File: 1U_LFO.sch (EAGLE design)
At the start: 22 parts

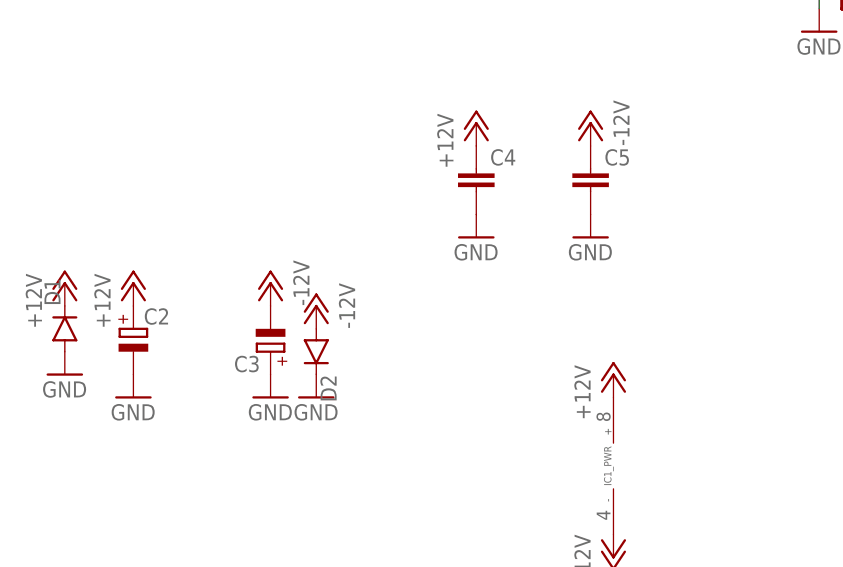
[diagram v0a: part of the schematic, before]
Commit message: 1U LFO
Basic Low Frequency Oscillator
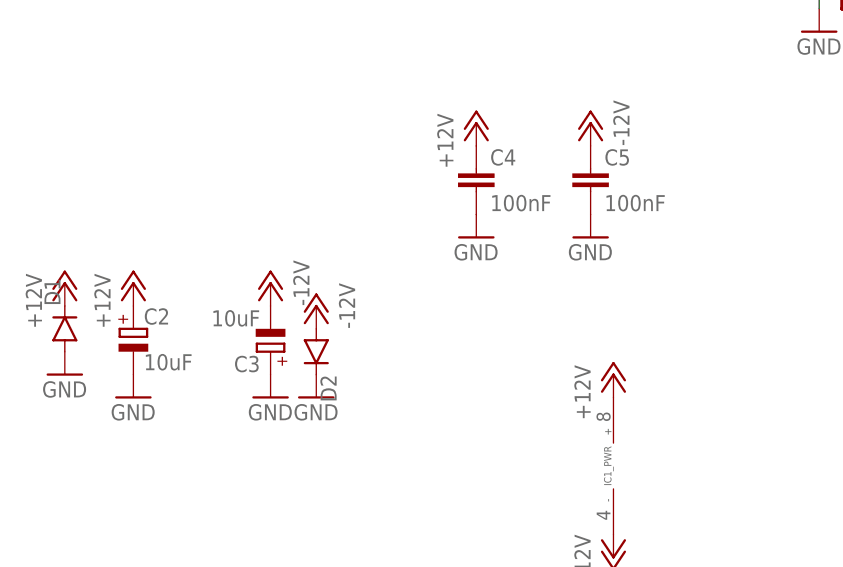
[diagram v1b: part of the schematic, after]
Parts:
- C2, C3: value (none) -> 10uF
- C4, C5: value (none) -> 100nF
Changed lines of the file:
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@@
 <?xml version="1.0" encoding="utf-8"?>
 <!DOCTYPE eagle SYSTEM "eagle.dtd">
-<eagle version="7.5.0">
+<eagle version="8.1.1">
 <drawing>
 <settings>
@@
 <part name="P-2" library="supply1" deviceset="-12V" device=""/>
 <part name="P-3" library="supply1" deviceset="-12V" device=""/>
-<part name="C2" library="dp_devices" deviceset="CAPACITOR_POL" device="-CASE_B"/>
-<part name="C3" library="dp_devices" deviceset="CAPACITOR_POL" device="-CASE_B"/>
+<part name="C2" library="dp_devices" deviceset="CAPACITOR_POL" device="-CASE_B" value="10uF"/>
+<part name="C3" library="dp_devices" deviceset="CAPACITOR_POL" device="-CASE_B" value="10uF"/>
 <part name="D1" library="SparkFun-DiscreteSemi" deviceset="DIODE" device="SOD123"/>
 <part name="D2" library="SparkFun-DiscreteSemi" deviceset="DIODE" device="SOD123"/>
-<part name="C4" library="SparkFun-Passives" deviceset="CAP" device="0603-CAP"/>
-<part name="C5" library="SparkFun-Passives" deviceset="CAP" device="0603-CAP"/>
+<part name="C4" library="SparkFun-Passives" deviceset="CAP" device="0603-CAP" value="100nF"/>
+<part name="C5" library="SparkFun-Passives" deviceset="CAP" device="0603-CAP" value="100nF"/>
 <part name="P+4" library="supply1" deviceset="+12V" device=""/>
 <part name="P+5" library="supply1" deviceset="+12V" device=""/>
